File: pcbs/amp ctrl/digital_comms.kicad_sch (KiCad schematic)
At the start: 51 parts, among them J15 RJ45_Shielded, J17 RJ45_Shielded, J88 RJ45_Shielded, Q33 MMBT3904, Q34 MMBT3904, Q35 MMBT3906, U21 74LVC2G17, U47 74LVC2G17, U62 FIN1028, U63 FIN1028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

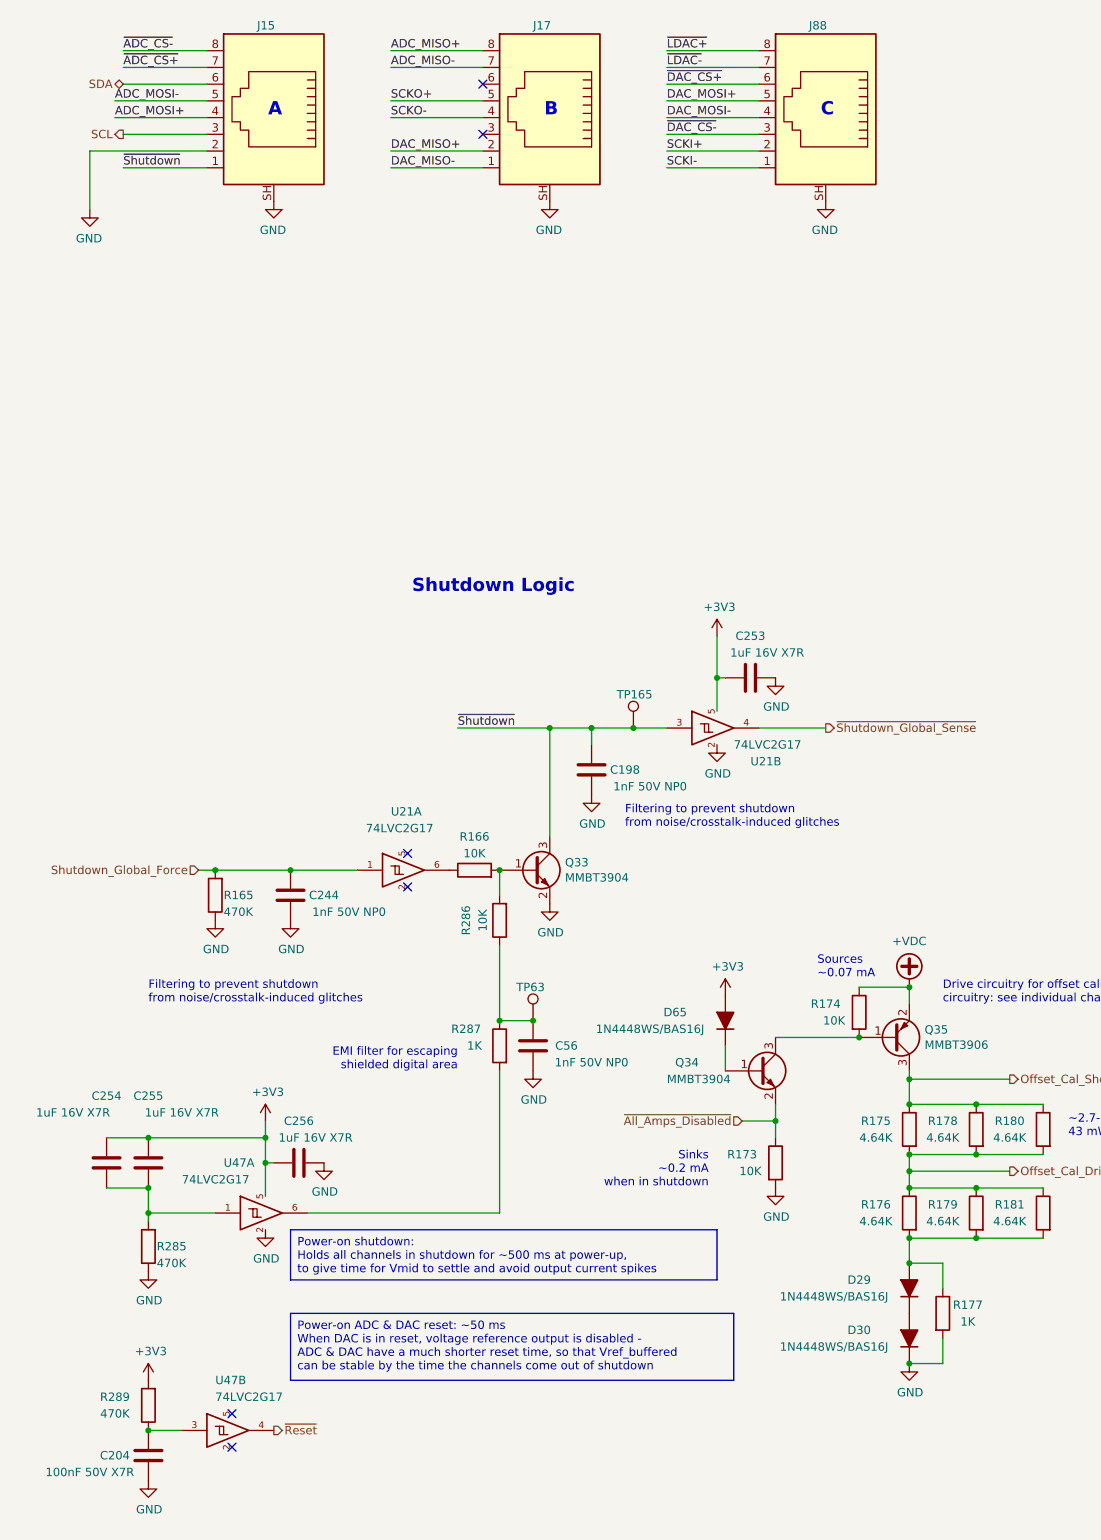
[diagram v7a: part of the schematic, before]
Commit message: Corrected power-up behavior
Backplane: Inverted polarity of Shutdown_Force (now Power_Enable_FPGA), to keep amps powered off until software starts: fixes #23
Backplane: Routed Shutdown_Force to unused pin 3 on RJ45 jack B to amp boards: fixes #23
Backplane: Added pull-up and pull-down resistors to fanout buffer inputs, to keep SCK & ~LDAC signals in proper state during power-on: fixes #23
Amp control: Added transistor to reset DAC & ADC from pin 3 of RJ45 jack B
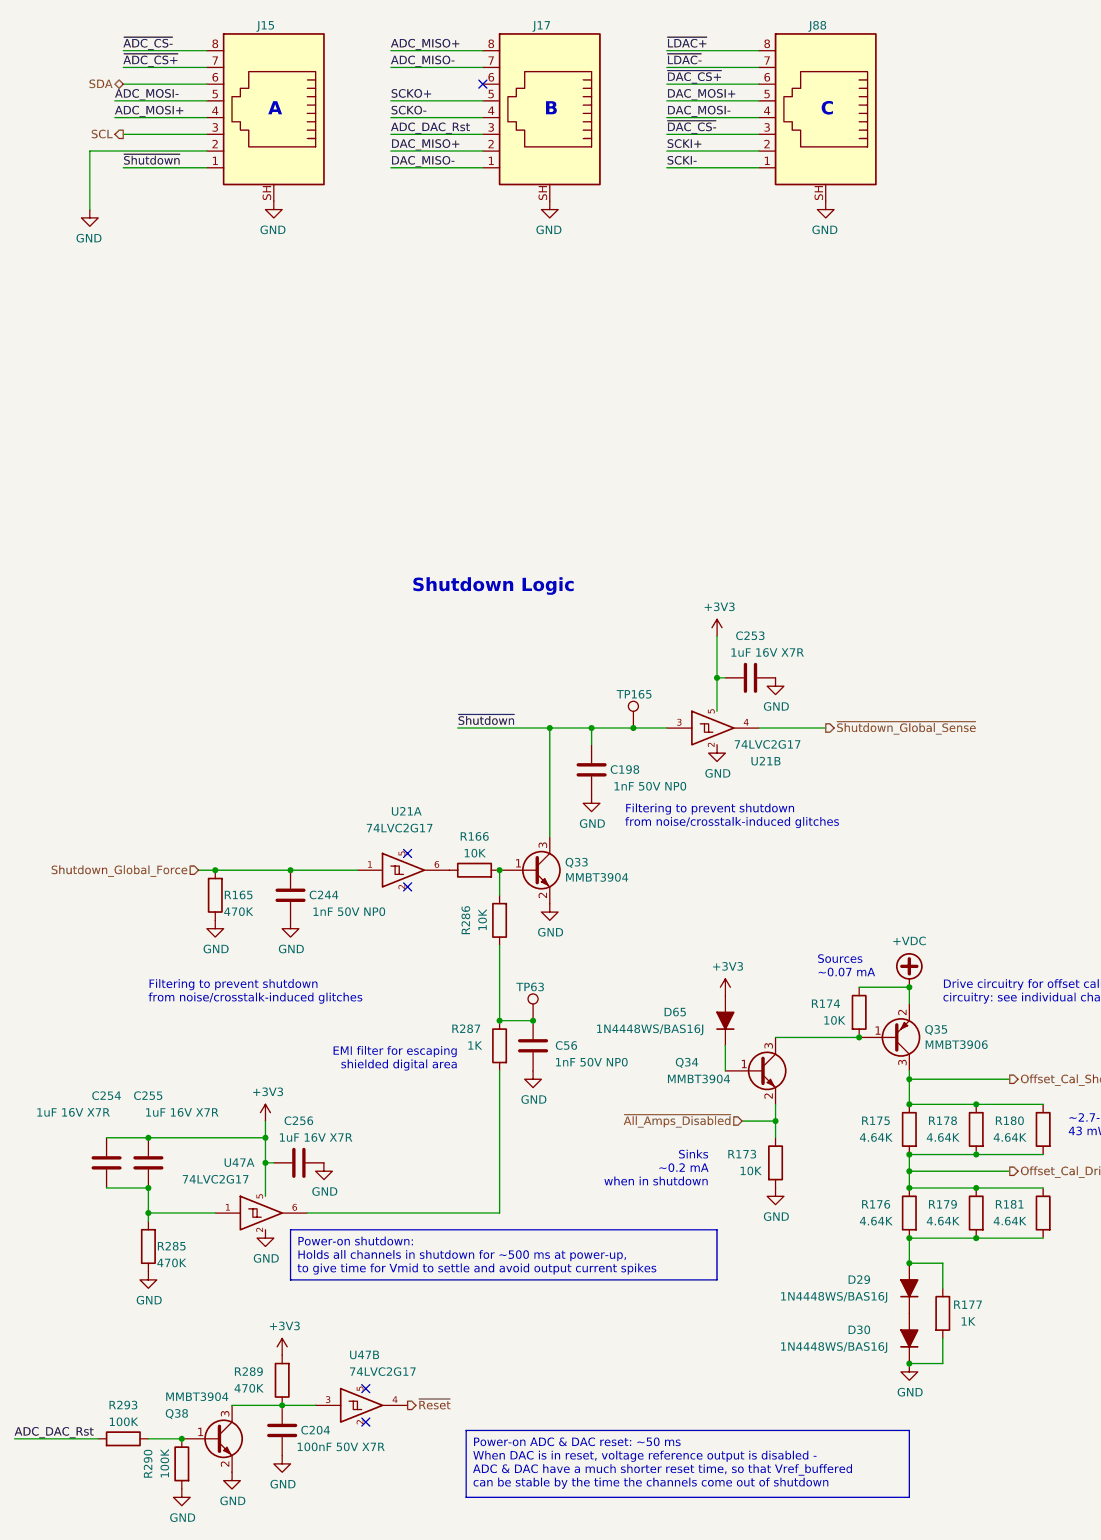
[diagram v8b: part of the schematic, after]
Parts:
- added Q38: MMBT3904, Don_std:SOT-23, symbol Transistor_BJT:MMBT3904
- added R290, R293: 100K, Resistor_SMD:R_0805_2012Metric, symbol Device:R
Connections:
- net GND: now also Q38.2 (E), R290.2
- net ADC_DAC_Rst: now reaches J17.3
- net ADC_DAC_Rst: now also R293.2
- net at C204.2, R289.1, U47.3: now also Q38.3 (C)
- new net: Q38.1 (B), R290.1, R293.1
- no-connect marks 16 -> 15
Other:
- moved on the sheet: C204, R289, U47B
